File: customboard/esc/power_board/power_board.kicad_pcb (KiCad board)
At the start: 4 copper layers, 44 x 44 mm, 107 parts, among them J1 Conn_01x08_MountingPin, J10 Conn_01x03_Pin, J2 Conn_01x01, J3 Conn_01x01, J4 Conn_01x03_Pin, J5 Conn_01x03_Pin, J6 Conn_01x03_Pin, Q1 BSC010N04LS6, Q10 BSC010N04LS6, Q11 BSC010N04LS6, Q12 BSC010N04LS6, Q13 BSC010N04LS6, Q14 BSC010N04LS6, Q15 BSC010N04LS6, Q16 BSC010N04LS6, Q17 BSC010N04LS6, Q18 BSC010N04LS6, Q19 BSC010N04LS6, Q2 BSC010N04LS6, Q20 BSC010N04LS6, Q21 BSC010N04LS6, Q22 BSC010N04LS6, Q23 BSC010N04LS6, Q24 BSC010N04LS6, Q3 BSC010N04LS6, Q4 BSC010N04LS6, Q5 BSC010N04LS6, Q6 BSC010N04LS6, Q7 BSC010N04LS6, Q8 BSC010N04LS6, Q9 BSC010N04LS6, U2 AP7381-50SA-7, U3 AP7381-33SA-7, U4 AP7381-50SA-7, U5 AP7381-50SA-7, U6 AP7381-50SA-7, U7 AP7381-33SA-7

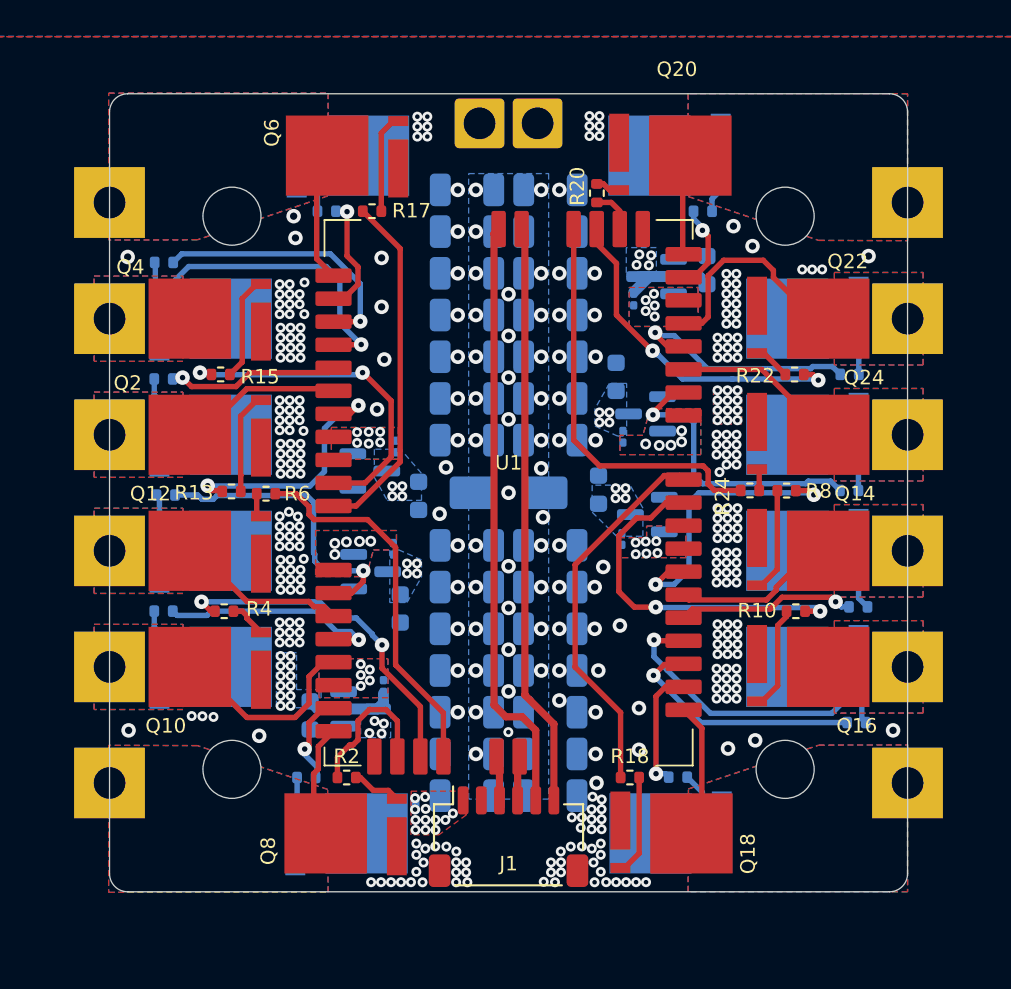
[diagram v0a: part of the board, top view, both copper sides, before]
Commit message: footprint fixes
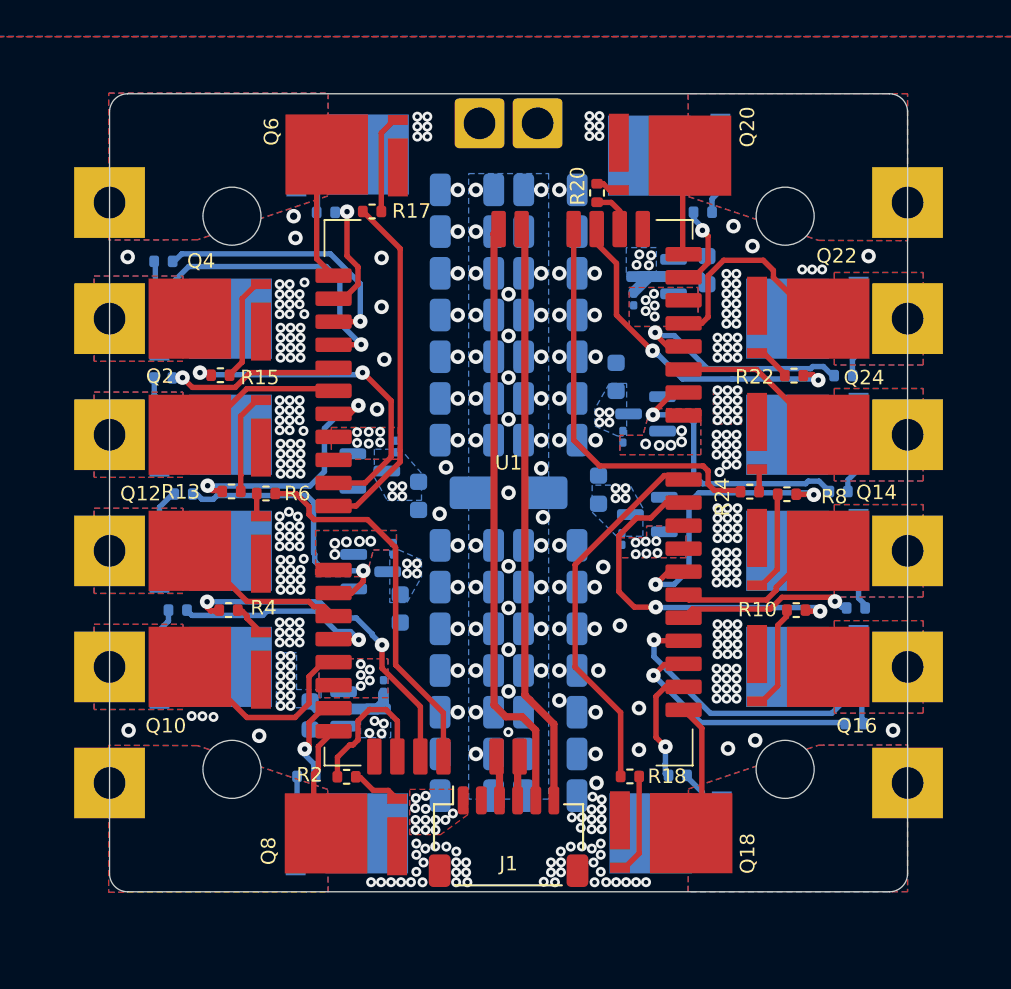
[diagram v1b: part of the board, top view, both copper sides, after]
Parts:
- moved R5 0.98 mm to (104.1, 92.1)
- moved R3 0.79 mm to (103.8, 98.5)
- moved R23 0.58 mm to (140.2, 91.9)
- moved R21 0.35 mm to (140.5, 85.5)
- moved R4 0.25 mm to (106.6, 98.5)
- moved R8 0.20 mm to (137.3, 92.1)
- moved R7 0.14 mm to (141.2, 98.3)
- moved R9 0.13 mm to (141.1, 104.7)
- moved R11 0.10 mm to (131.3, 107.6)
- moved R16 0.08 mm to (111.9, 76.5)
- moved R24 0.07 mm to (135.3, 91.9)
- moved R14 0.07 mm to (103.0, 79.2)
- moved R22 0.07 mm to (137.7, 85.5)
- moved Q5 0.06 mm to (113.1, 73.3)
- moved Q6 0.06 mm to (113.1, 73.3)
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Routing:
- net /EscMotor2/GHA: track 16.6 -> 15.7 mm
- net /EscMotor2/GHB: track 12.5 -> 11.8 mm
- net +BATT: track 0.66 -> 0.00 mm
- net /EscMotor4/GHA: track 16.1 -> 15.5 mm

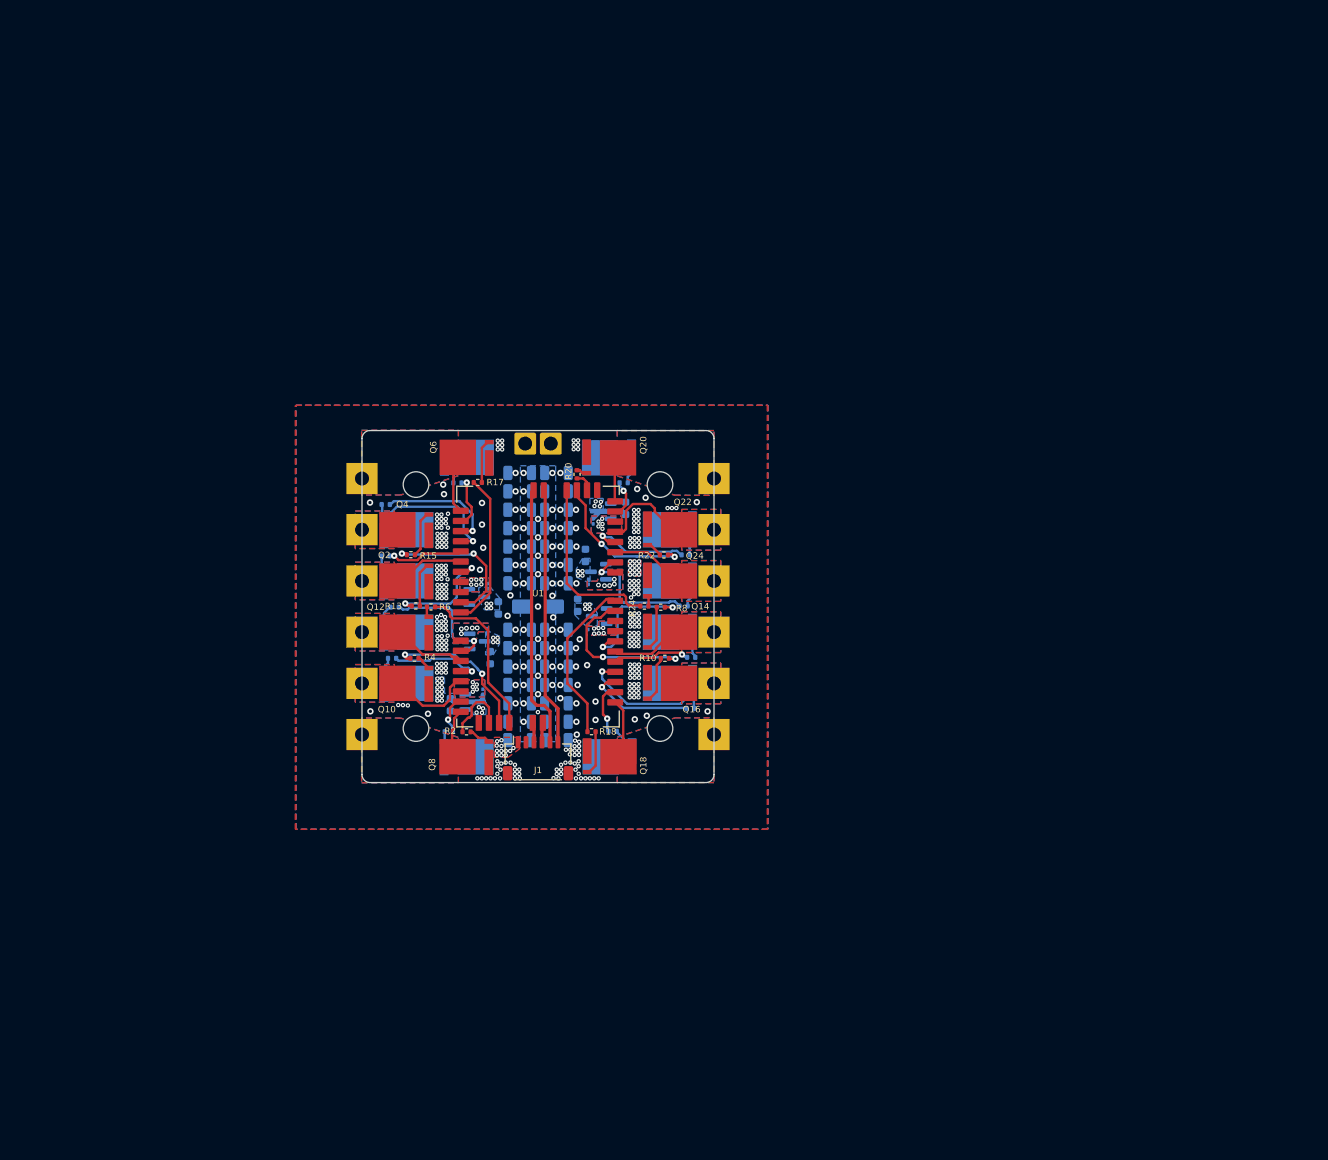
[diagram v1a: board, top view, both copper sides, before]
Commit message: power board done, minor fixes in logic board
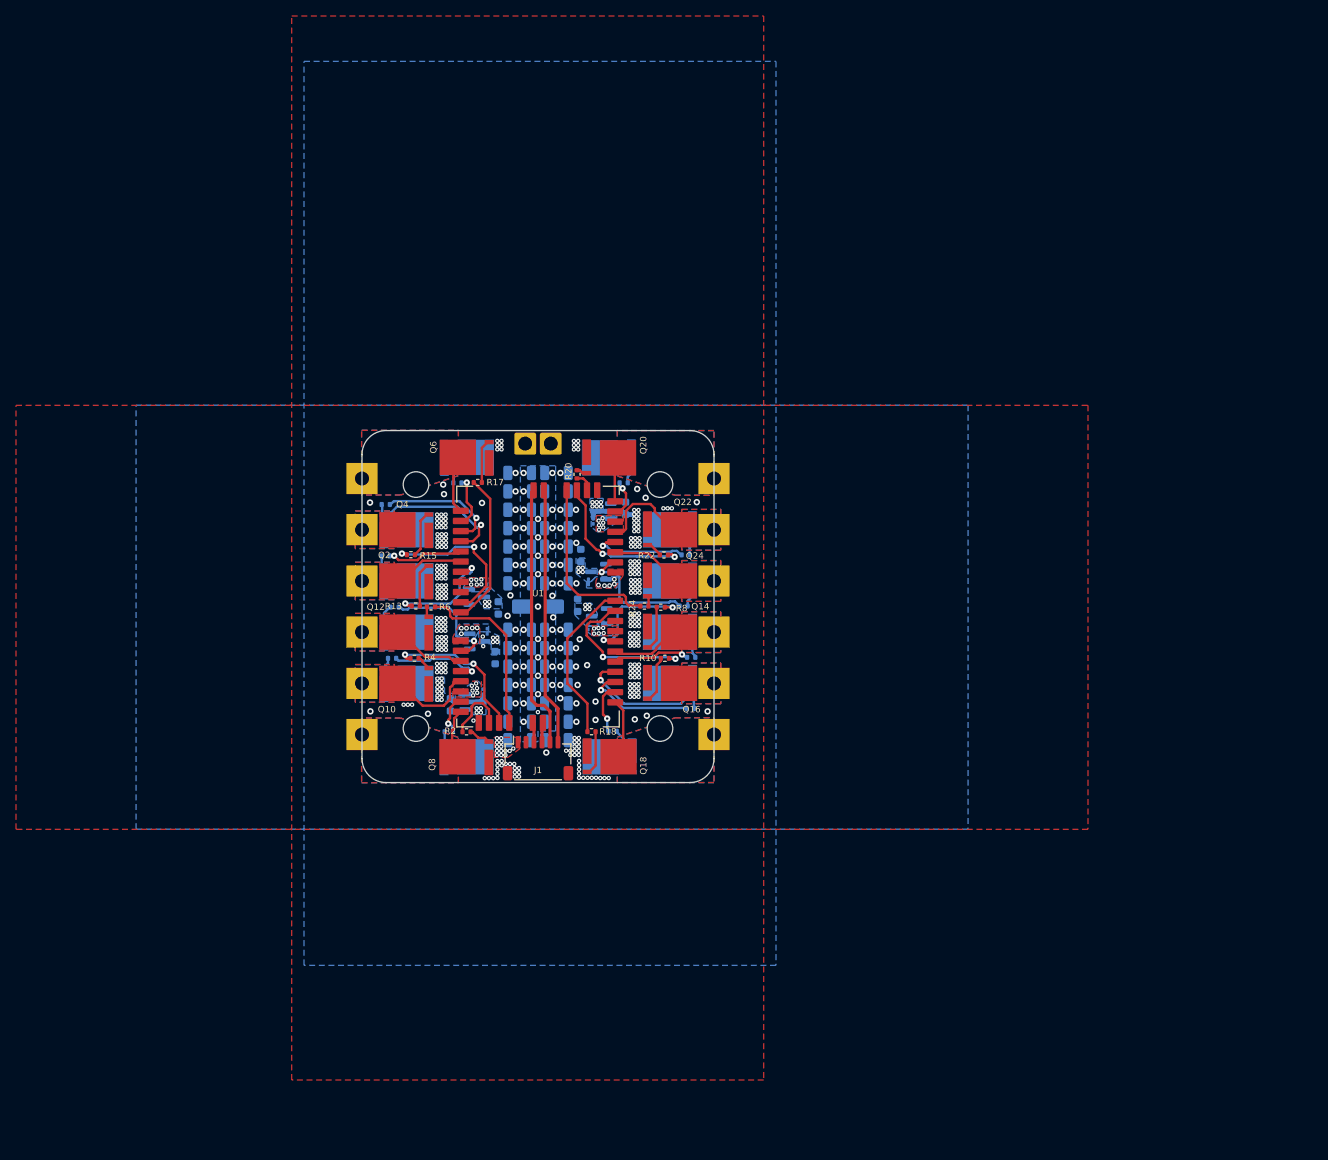
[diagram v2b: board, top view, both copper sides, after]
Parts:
- moved C8 0.62 mm to (116.7, 98.4)
- moved C39 0.58 mm to (127.3, 85.6)
- moved C11 0.18 mm to (115.6, 89.5)
- turned C23 to 0 degrees
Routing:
- net /EscMotor1/MOTORB: track 18.5 -> 20.1 mm
- net /EscMotor3/GLC: track 15.8 -> 14.6 mm
- net /EscMotor2/GLA: track 20.7 -> 21.8 mm
- net /EscMotor1/GLB: track 18.9 -> 19.8 mm
- net /EscMotor4/GLB: track 18.8 -> 19.6 mm
- net /EscMotor4/GHB: track 12.9 -> 12.1 mm
- net /EscMotor3/GLB: track 19.8 -> 19.1 mm
- net GND: track 11.0 -> 11.1 mm, vias 220 -> 215
- net /5V_3: vias 5 -> 6
- net /5V_2: vias 5 -> 6
- net +BATT: vias 160 -> 163
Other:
- outline, holes or cut-outs redrawn

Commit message: stuff
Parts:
- moved R13 29.2 mm to (134.7, 100.1)
- moved C1 29.1 mm to (147.7, 83.3)
- moved C12 29.1 mm to (152.3, 107.5)
- moved C13 29.1 mm to (152.3, 105.2)
- moved C16 29.1 mm to (152.3, 102.9)
- moved C2 29.1 mm to (147.7, 87.9)
- moved C21 29.1 mm to (152.3, 114.4)
- moved C23 29.1 mm to (152.3, 116.7)
- moved C24 29.1 mm to (152.3, 112.1)
- moved C25 29.1 mm to (152.3, 97.1)
- moved C27 29.1 mm to (147.7, 90.2)
- moved C30 29.1 mm to (147.7, 92.5)
- moved C32 29.1 mm to (152.3, 109.8)
- moved C35 29.1 mm to (155.0, 99.8)
- moved C5 29.1 mm to (152.3, 94.8)
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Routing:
- net GND: vias 215 -> 204
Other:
- board size 44 x 44 mm -> 44 x 46.5 mm
- board text added: "+"
- board text added: "-"

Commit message: 4x esc fixes
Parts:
- moved R22 0.68 mm to (165.1, 93.5)
- moved R9 0.64 mm to (168.4, 112.7)
- moved R6 0.54 mm to (137.2, 100.1)
- moved R14 0.51 mm to (131.5, 87.2)
- moved R7 0.41 mm to (168.7, 106.4)
- moved R24 0.41 mm to (162.9, 99.9)
- moved Q13 0.30 mm to (166.2, 103.2)
- moved Q14 0.30 mm to (166.2, 103.2)
- moved Q15 0.30 mm to (166.2, 109.6)
- moved Q16 0.30 mm to (166.2, 109.6)
- moved Q21 0.30 mm to (166.2, 90.4)
- moved Q22 0.30 mm to (166.2, 90.4)
- moved Q23 0.30 mm to (166.2, 96.8)
- moved Q24 0.30 mm to (166.2, 96.8)
- moved Q1 0.30 mm to (133.8, 96.8)
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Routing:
- net /EscMotor2/MOTORB: track 10.3 -> 11.8 mm
- net /EscMotor3/MOTORC: track 8.11 -> 9.49 mm
- net /EscMotor4/MOTORB: track 12.9 -> 11.7 mm
- net /EscMotor4/MOTORA: track 8.55 -> 9.63 mm
- net /EscMotor4/GLB: track 19.6 -> 18.6 mm
- net /EscMotor2/MOTORA: track 8.50 -> 9.48 mm
- net /EscMotor2/GLB: track 18.8 -> 18.1 mm
- net /EscMotor1/MOTORC: track 7.97 -> 8.70 mm
- net /EscMotor1/GHB: track 15.2 -> 14.5 mm
- net /EscMotor3/GHB: track 14.0 -> 13.3 mm
- net /EscMotor1/MOTORB: track 20.1 -> 19.5 mm
- net /EscMotor2/GLA: track 21.8 -> 21.3 mm
- net /EscMotor3/GLB: track 19.1 -> 18.6 mm
- net /EscMotor3/GLC: track 14.6 -> 14.1 mm

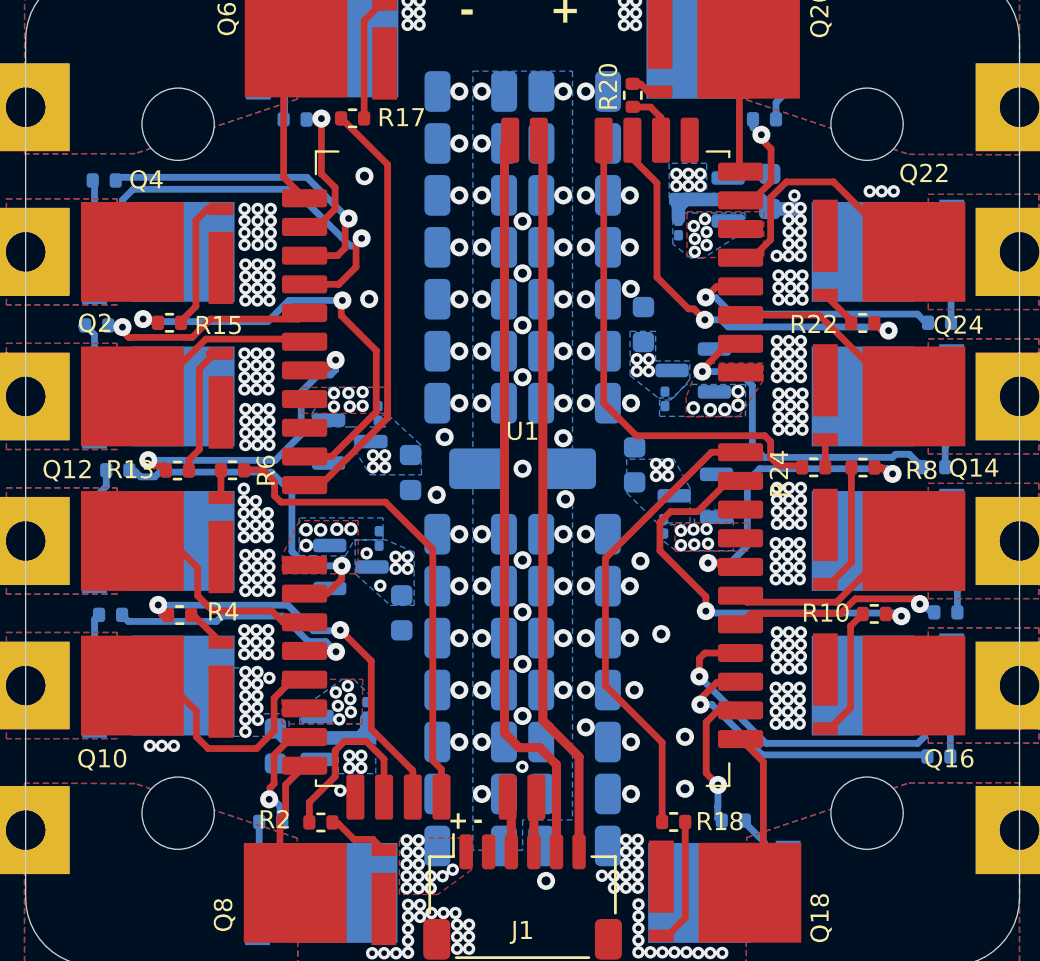
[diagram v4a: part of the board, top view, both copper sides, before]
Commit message: sot-89 regulator
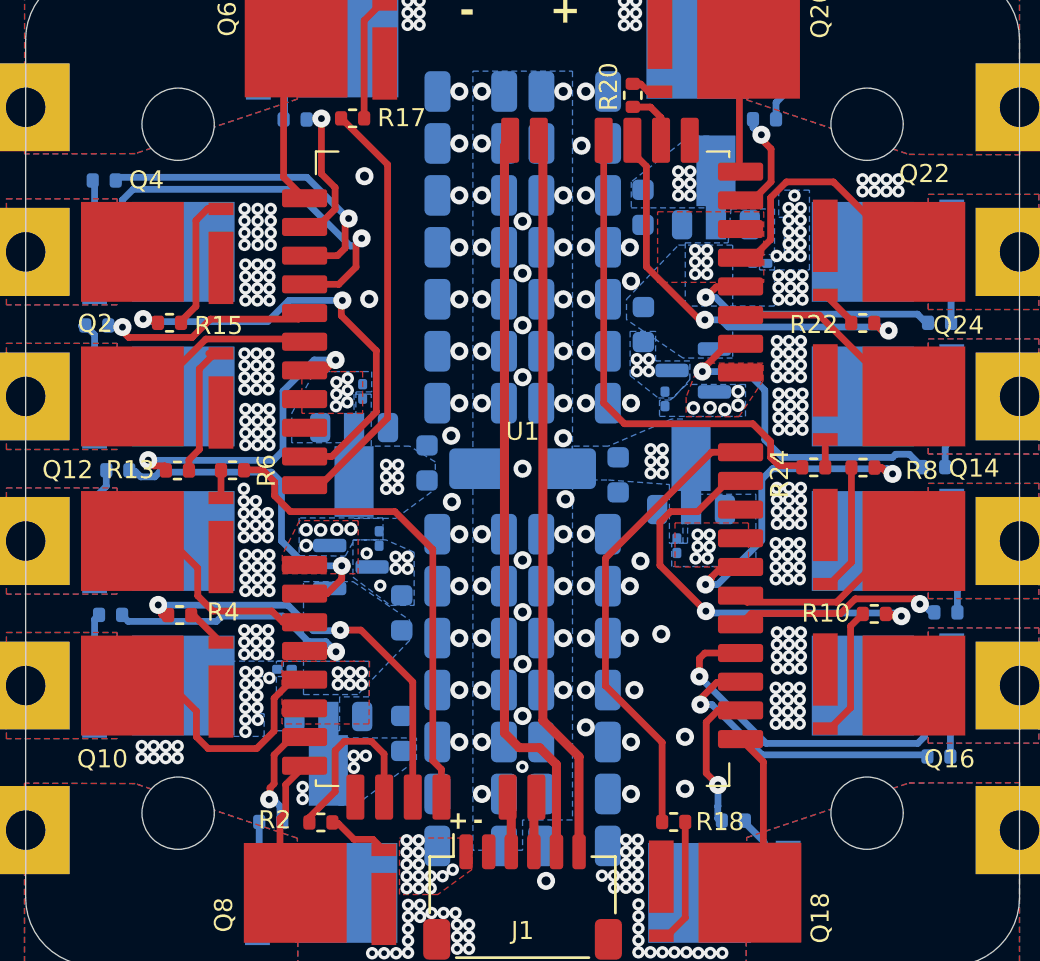
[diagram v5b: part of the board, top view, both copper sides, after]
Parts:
- removed U6: AP7381-50SA-7, Package_TO_SOT_SMD:SOT-23
- added U8: AP130-25Y, Package_TO_SOT_SMD:SOT-89-3, B.Cu at (142.5, 100.1)
- U2, U4, U5: value AP7381-50SA-7 -> AP130-25Y; footprint Package_TO_SOT_SMD:SOT-23 -> Package_TO_SOT_SMD:SOT-89-3
- moved C37 5.65 mm to (155.3, 88.4), turned to 90 degrees
- moved C33 5.62 mm to (144.7, 111.7), turned to -90 degrees
- moved C34 4.05 mm to (139.5, 108.9), turned to 180 degrees
- moved C38 3.93 mm to (160.5, 90.9), turned to 0 degrees
- moved U4 1.35 mm to (157.5, 99.9), turned to 90 degrees
- moved C11 1.18 mm to (142.9, 96.6)
- moved U2 1.09 mm to (141.4, 112.9), turned to -90 degrees
- moved C36 1.04 mm to (156.8, 103.4)
- moved U5 0.92 mm to (158.6, 87.2), turned to 90 degrees
- moved C35 0.85 mm to (154.2, 100.3), turned to 90 degrees
- moved C10 0.84 mm to (145.8, 99.7), turned to -90 degrees
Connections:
- C39 pad 1: +BATT -> /5V_3
- C8 pad 1: +BATT -> /5V_2
- U2 pad 1: +BATT -> /5V_2
- U2 pad 2: /5V_2 -> GND
- U2 pad 3: GND -> +BATT
- U3 pad 1: +BATT -> /5V_2
- U4 pad 1: +BATT -> /5V_4
- U4 pad 2: /5V_4 -> GND
- U4 pad 3: GND -> +BATT
- U5 pad 1: +BATT -> /5V_3
- U5 pad 2: /5V_3 -> GND
- U5 pad 3: GND -> +BATT
- U7 pad 1: +BATT -> /5V_3
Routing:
- net GND: track 11.1 -> 0.00 mm, vias 204 -> 208
- net /EscMotor3/GLC: track 14.1 -> 14.9 mm
- net /EscMotor2/GLB: track 18.1 -> 18.6 mm
- net +BATT: vias 163 -> 173
